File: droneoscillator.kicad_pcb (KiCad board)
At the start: 2 copper layers, 29.5 x 114.3 mm, 48 parts, among them J1 Conn_01x02, J2 Conn_01x03, Q1 BC337, Q2 BC337, Q3 BC337, Q4 BC337, U1 NE5532

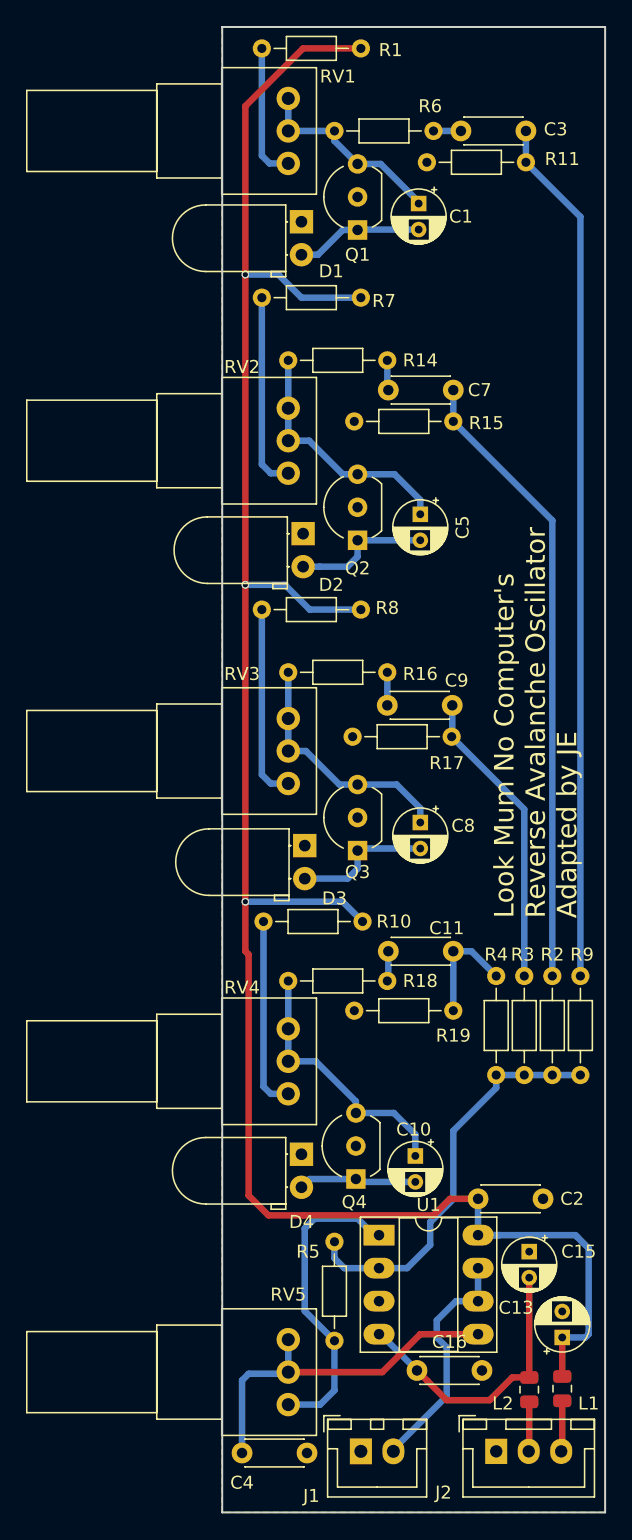
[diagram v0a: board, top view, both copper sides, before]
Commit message: added front panel, adjusted PCB slightly to improve front panel real estate
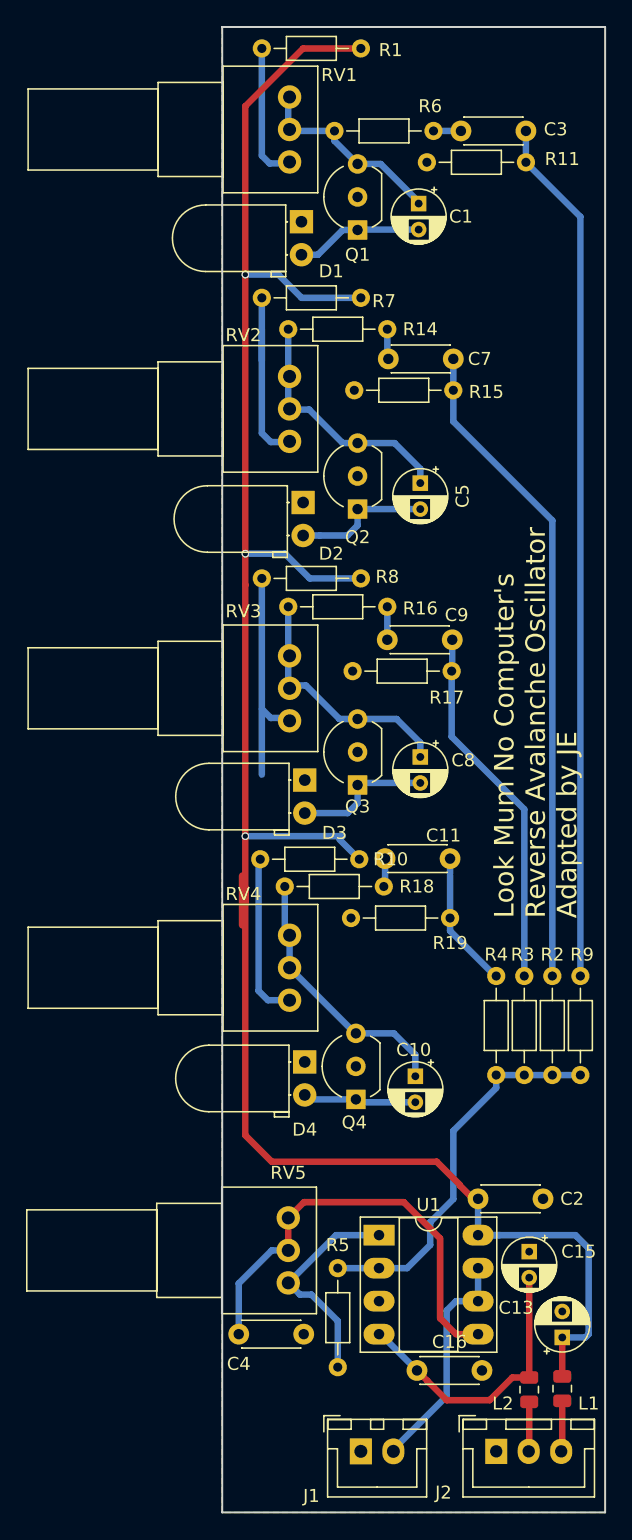
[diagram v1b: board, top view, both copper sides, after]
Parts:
- moved RV5 9.37 mm to (136.4, 130.5)
- moved C4 9.15 mm to (132.6, 139.4)
- moved R18 7.27 mm to (143.8, 105.0)
- moved RV4 7.20 mm to (136.5, 108.8)
- moved C11 7.13 mm to (148.8, 102.9)
- moved R19 7.13 mm to (148.8, 107.4)
- moved D4 7.11 mm to (137.7, 118.5)
- moved C10 6.13 mm to (146.2, 119.6)
- moved Q4 6.13 mm to (141.6, 121.4)
- moved R16 5.04 mm to (144.0, 83.5)
- moved C8 5.04 mm to (146.6, 95.0)
- moved C9 5.04 mm to (149.0, 86.0)
- moved D3 5.04 mm to (137.7, 96.8)
- moved Q3 5.04 mm to (141.7, 97.2)
- moved R17 5.04 mm to (149.0, 88.4)
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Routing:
- net Net-(R5-Pad1): track 24.0 -> 17.1 mm
- net Net-(C4-Pad1): track 27.8 -> 34.2 mm
- net /OscC: track 23.2 -> 28.2 mm
- net Net-(R8-Pad2): track 14.3 -> 16.7 mm
- net /OscB: track 48.2 -> 50.7 mm
- net /OscD: track 8.52 -> 10.4 mm
- net Net-(R2-Pad1): track 31.4 -> 29.5 mm
- net +12V: track 167.6 -> 169.2 mm
- net Net-(R10-Pad2): track 14.1 -> 13.2 mm
- net Net-(C10-Pad2): track 9.12 -> 8.22 mm
- net Net-(J1-Pad2): track 18.4 -> 17.8 mm

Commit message: Minor schematic changes after prototype build, cleaned up PCB design
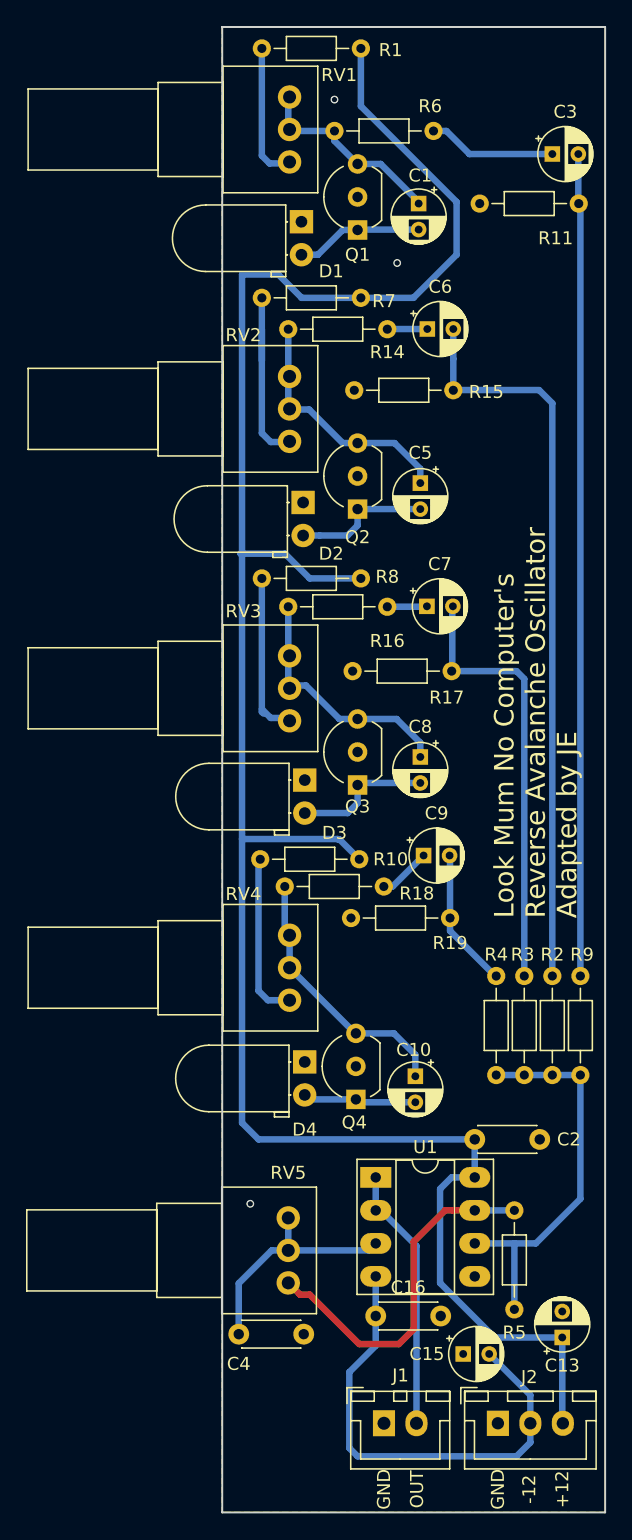
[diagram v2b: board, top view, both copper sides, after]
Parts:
- removed C11: 100n, Capacitor_THT:C_Disc_D4.3mm_W1.9mm_P5.00mm
- removed L1, L2: 786-7068, Inductor_SMD:L_0805_2012Metric
- added C6: 2u2, Capacitor_THT:CP_Radial_D4.0mm_P2.00mm, F.Cu at (147.1, 62.1)
- C3, C7, C9: value 100n -> 2u2; footprint Capacitor_THT:C_Disc_D4.3mm_W1.9mm_P5.00mm -> Capacitor_THT:CP_Radial_D4.0mm_P2.00mm
- R1, R10, R7, R8: value 2K -> 1K
- RV1, RV2, RV3, RV4: value 100K -> 50K
- moved C7 19.1 mm to (147.1, 83.4), turned to 0 degrees
- moved R5 18.2 mm to (153.8, 129.9), turned to 270 degrees
- moved C9 16.7 mm to (146.8, 102.6), turned to 0 degrees
- moved C15 9.37 mm to (149.9, 141.0), turned to 0 degrees
- moved C16 5.26 mm to (143.1, 138.0)
- moved R11 5.16 mm to (158.8, 52.5)
- moved C2 4.58 mm to (150.7, 124.5)
- moved U1 4.45 mm to (143.1, 127.4)
- moved J1 2.80 mm to (143.8, 146.3)
- moved C3 2.70 mm to (156.7, 48.6), turned to 0 degrees
- moved J2 2.16 mm to (152.5, 146.3)
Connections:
- C3 pad 1: /OscA -> Net-(C3-Pad1)
- C3 pad 2: Net-(C3-Pad2) -> /OscA
- C7 pad 1: /OscB -> Net-(C7-Pad1)
- C7 pad 2: Net-(C7-Pad2) -> /OscC
- C9 pad 1: /OscC -> Net-(C9-Pad1)
- C9 pad 2: Net-(C9-Pad2) -> /OscD
- J2 pad 2: Net-(J2-Pad2) -> -12VA
- J2 pad 3: Net-(J2-Pad3) -> +12V
- R14 pad 1: Net-(C7-Pad2) -> Net-(C6-Pad1)
- R16 pad 1: Net-(C9-Pad2) -> Net-(C7-Pad1)
- R18 pad 1: Net-(C11-Pad2) -> Net-(C9-Pad1)
- R6 pad 1: Net-(C3-Pad2) -> Net-(C3-Pad1)
- U1 pad 1: Net-(R5-Pad1) -> Net-(J1-Pad2)
- U1 pad 2: Net-(R2-Pad1) -> Net-(J1-Pad2)
- U1 pad 3: GND -> Net-(C4-Pad1)
- U1 pad 5: Net-(C4-Pad1) -> GND
- U1 pad 6: Net-(J1-Pad2) -> Net-(R2-Pad1)
- U1 pad 7: Net-(J1-Pad2) -> Net-(R5-Pad1)
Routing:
- net Net-(C4-Pad1): track 34.2 -> 18.2 mm
- net -12VA: track 22.1 -> 36.8 mm
- net Net-(R5-Pad1): track 17.1 -> 27.6 mm
- net Net-(C3-Pad1): track 0.00 -> 9.88 mm
- net /OscB: track 50.7 -> 56.8 mm
- net /OscC: track 28.2 -> 33.7 mm
- net Net-(R8-Pad2): track 16.7 -> 12.1 mm
- net Net-(C9-Pad1): track 0.00 -> 4.16 mm
- net Net-(J2-Pad3): track 3.92 -> 0.00 mm
- net Net-(J2-Pad2): track 3.83 -> 0.00 mm
- net /OscA: track 66.8 -> 63.3 mm
- net Net-(C6-Pad1): track 0.00 -> 3.09 mm
- net Net-(C7-Pad1): track 0.00 -> 3.06 mm
- net Net-(J1-Pad2): track 17.8 -> 20.5 mm
- net +12V: track 169.2 -> 171.9 mm, vias 3 -> 0
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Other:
- board text added: "+12"
- board text added: "-12"
- board text added: "GND"
- board text added: "OUT"

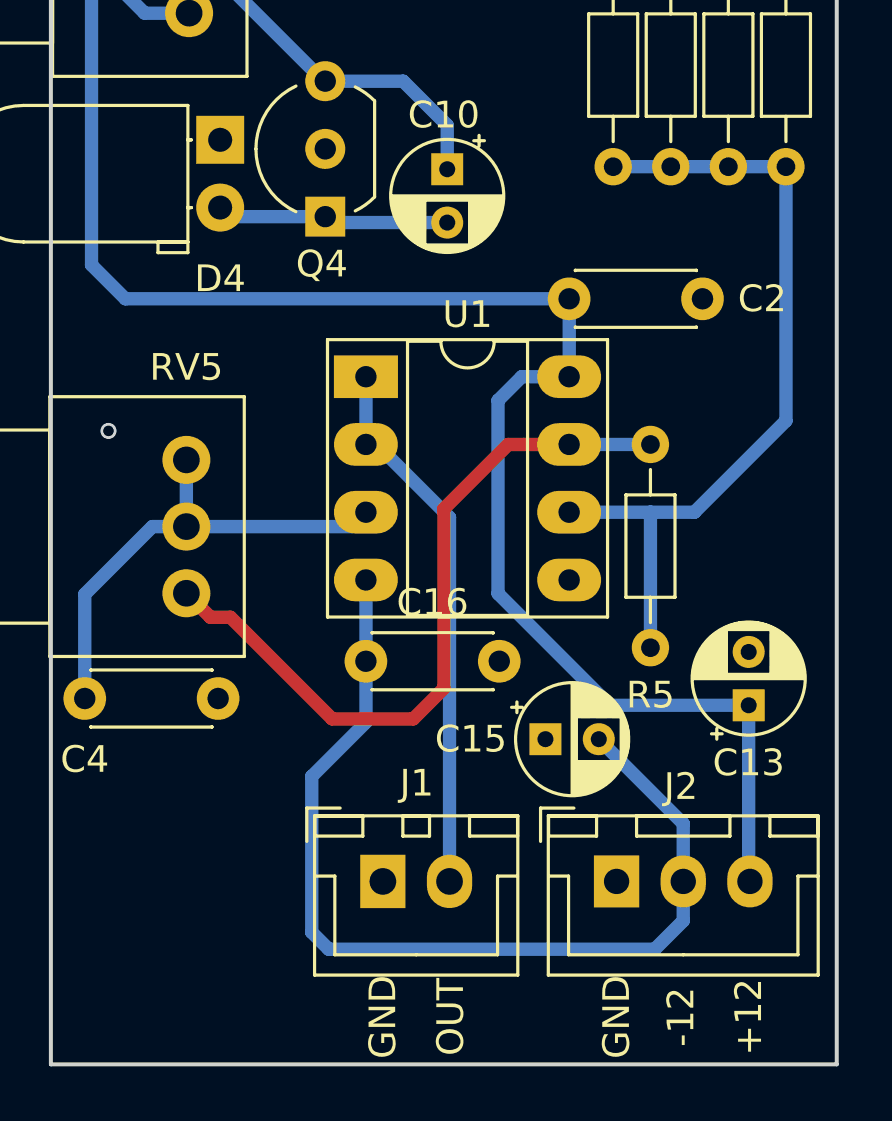
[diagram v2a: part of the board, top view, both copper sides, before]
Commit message: added input filtering to power supply
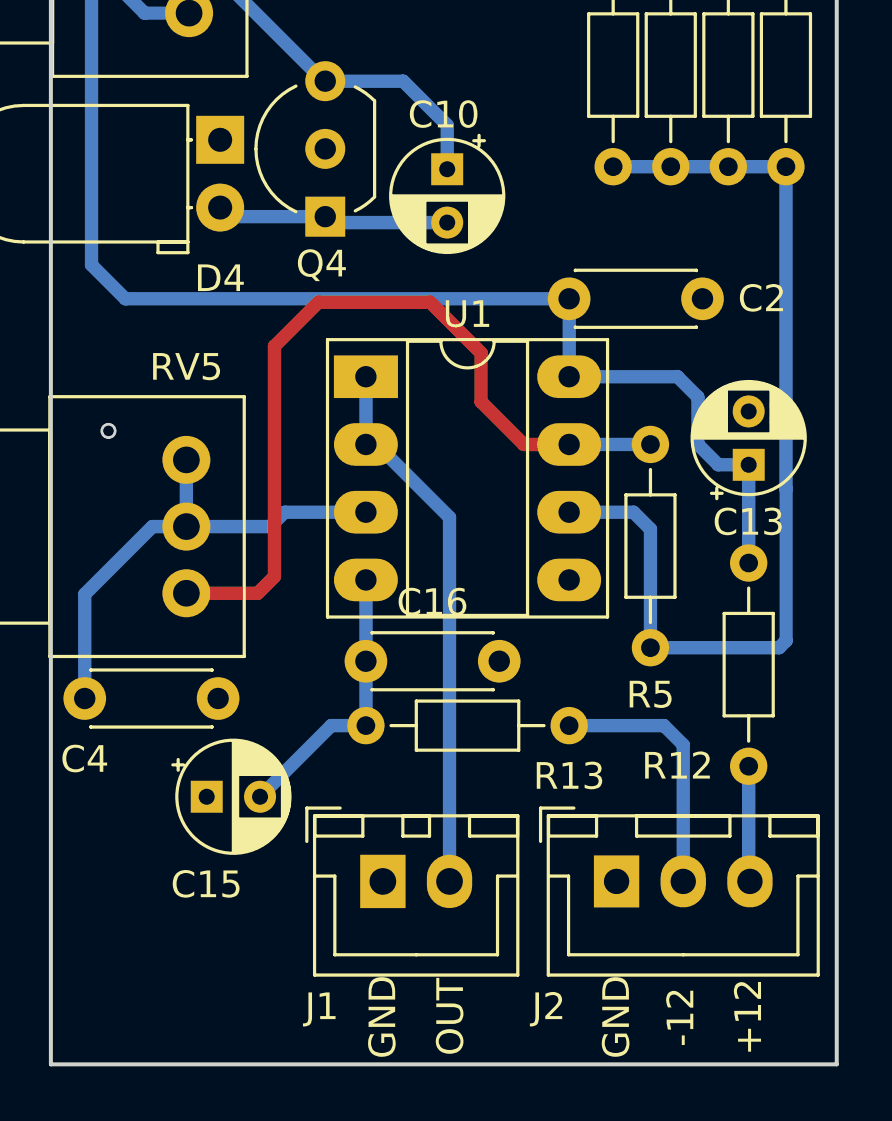
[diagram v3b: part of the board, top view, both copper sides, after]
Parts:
- added R12: 10R, Resistor_THT:R_Axial_DIN0204_L3.6mm_D1.6mm_P7.62mm_Horizontal, F.Cu at (157.5, 134.4)
- added R13: 10R, Resistor_THT:R_Axial_DIN0204_L3.6mm_D1.6mm_P7.62mm_Horizontal, F.Cu at (150.7, 140.5)
- moved C15 12.9 mm to (137.2, 143.1)
- moved C13 9.02 mm to (157.5, 130.7)
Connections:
- J2 pad 2: -12VA -> Net-(J2-Pad2)
- J2 pad 3: +12V -> Net-(J2-Pad3)
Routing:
- net -12VA: track 36.8 -> 10.5 mm
- net +12V: track 171.9 -> 156.7 mm
- net Net-(J2-Pad2): track 0.00 -> 9.70 mm
- net Net-(R2-Pad1): track 30.6 -> 37.2 mm
- net Net-(J2-Pad3): track 0.00 -> 4.34 mm
- net Net-(R5-Pad1): track 27.6 -> 30.3 mm

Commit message: pcb and schematic tweaks
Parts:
- RV5: value 100K -> 50K
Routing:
- net Net-(J1-Pad2): track 20.5 -> 21.5 mm
- net Net-(R5-Pad1): track 30.3 -> 30.8 mm
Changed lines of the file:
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@@
     (thickness 1.6)
     (drawings 10)
-    (tracks 167)
+    (tracks 170)
     (zones 0)
     (modules 48)
@@
       (effects (font (size 1 1) (thickness 0.15)))
     )
-    (fp_text value 100K (at 0 3.5 180) (layer F.Fab)
+    (fp_text value 50K (at 0 3.5 180) (layer F.Fab)
       (effects (font (size 1 1) (thickness 0.15)))
     )
@@
     (descr "C, Disc series, Radial, pin pitch=5.00mm, , diameter*width=4.3*1.9mm^2, Capacitor, http://www.vishay.com/docs/45233/krseries.pdf")
     (tags "C Disc series Radial pin pitch 5.00mm  diameter 4.3mm width 1.9mm Capacitor")
-    (fp_text reference C16 (at 2.5 -2.2) (layer F.SilkS)
+    (fp_text reference C16 (at -2.54 0) (layer F.SilkS)
       (effects (font (size 1 1) (thickness 0.15)))
     )
@@
   (segment (start 140.339 101.378) (end 141.863 102.902) (width 0.5) (layer B.Cu) (net 3))
   (segment (start 137.414 59.704) (end 141.986 59.704) (width 0.5) (layer B.Cu) (net 3))
-  (segment (start 157.48 146.257) (end 157.527 146.304) (width 0.5) (layer B.Cu) (net 32))
   (segment (start 150.749 124.46) (end 150.749 127.381) (width 0.5) (layer B.Cu) (net 3))
   (segment (start 146.036 59.704) (end 141.986 59.704) (width 0.5) (layer B.Cu) (net 3))
@@
   (segment (start 147.447 126.492) (end 145.542 124.587) (width 0.5) (layer F.Cu) (net 18))
   (segment (start 145.542 124.587) (end 141.351 124.587) (width 0.5) (layer F.Cu) (net 18))
-  (segment (start 141.351 124.587) (end 139.7 126.238) (width 0.5) (layer F.Cu) (net 18))
-  (segment (start 139.7 126.238) (end 139.7 134.874) (width 0.5) (layer F.Cu) (net 18))
-  (segment (start 139.074 135.5) (end 136.398 135.5) (width 0.5) (layer F.Cu) (net 18))
-  (segment (start 139.7 134.874) (end 139.074 135.5) (width 0.5) (layer F.Cu) (net 18))
   (segment (start 135.048 70.8) (end 135.69799 70.8) (width 0.5) (layer B.Cu) (net 19))
   (segment (start 134.366 62.117) (end 134.366 70.118) (width 0.5) (layer B.Cu) (net 19))
@@
   (segment (start 134.112 113.03) (end 134.832 113.75) (width 0.5) (layer B.Cu) (net 26))
   (segment (start 134.112 102.699) (end 134.112 113.03) (width 0.5) (layer B.Cu) (net 26))
-  (segment (start 143.529 129.921) (end 143.129 129.921) (width 0.5) (layer B.Cu) (net 27))
-  (segment (start 146.264 146.304) (end 146.264 132.656) (width 0.5) (layer B.Cu) (net 27))
-  (segment (start 146.264 132.656) (end 143.529 129.921) (width 0.5) (layer B.Cu) (net 27))
   (segment (start 143.129 127.381) (end 143.129 129.921) (width 0.5) (layer B.Cu) (net 27))
   (segment (start 147.574 46.863) (end 148.563949 46.863) (width 0.5) (layer B.Cu) (net 28))
@@
   (segment (start 144.428 105) (end 146.812 102.616) (width 0.5) (layer B.Cu) (net 31))
   (segment (start 143.75 105) (end 144.428 105) (width 0.5) (layer B.Cu) (net 31))
+  (segment (start 157.48 146.257) (end 157.527 146.304) (width 0.5) (layer B.Cu) (net 32))
   (segment (start 157.48 141.986) (end 157.48 146.257) (width 0.5) (layer B.Cu) (net 32))
   (segment (start 155.027 141.184) (end 155.027 146.304) (width 0.5) (layer B.Cu) (net 33))
   (segment (start 150.749 140.462) (end 154.305 140.462) (width 0.5) (layer B.Cu) (net 33))
   (segment (start 154.305 140.462) (end 155.027 141.184) (width 0.5) (layer B.Cu) (net 33))
+  (segment (start 137.670792 135.5) (end 137.679792 135.509) (width 0.5) (layer F.Cu) (net 18))
+  (segment (start 136.398 135.5) (end 137.670792 135.5) (width 0.5) (layer F.Cu) (net 18))
+  (segment (start 137.679792 135.509) (end 139.573 135.509) (width 0.5) (layer F.Cu) (net 18))
+  (segment (start 139.573 135.509) (end 140.081 135.001) (width 0.5) (layer F.Cu) (net 18))
+  (segment (start 140.081 135.001) (end 140.081 125.476) (width 0.5) (layer F.Cu) (net 18))
+  (segment (start 140.97 124.587) (end 141.351 124.587) (width 0.5) (layer F.Cu) (net 18))
+  (segment (start 140.081 125.476) (end 140.97 124.587) (width 0.5) (layer F.Cu) (net 18))
+  (segment (start 145.288 129.921) (end 143.129 129.921) (width 0.5) (layer B.Cu) (net 27))
+  (segment (start 146.264 146.304) (end 146.264 130.897) (width 0.5) (layer B.Cu) (net 27))
+  (segment (start 146.264 130.897) (end 145.288 129.921) (width 0.5) (layer B.Cu) (net 27))
   (zone (net 1) (net_name GND) (layer B.Cu) (hatch edge 0.508)
     (connect_pads (clearance 0.508))
